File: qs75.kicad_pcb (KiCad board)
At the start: 2 copper layers, 285 x 95.1 mm, 284 parts, among them J1 SWD, J2 SPI, J3 UART, J4 USB2.0, J5 PB14, SW1 SW_Push, SW10 1u, SW11 1u, SW12 1u, SW13 1u, SW14 1u, SW15 1u, SW16 1u, SW17 1u, SW18 1u, SW19 1u, SW2 1u, SW20 1u, SW21 1u, SW22 1u, SW23 1u, SW24 1u, SW25 1u, SW26 1u, SW27 1u, SW28 1u, SW29 1u, SW3 1u, SW30 1u, SW31 1u, SW32 1u, SW33 1u, SW34 1u, SW35 1u, SW36 1u, SW37 1u, SW38 1u, SW39 1u, SW4 1u, SW40 1u, SW41 1u, SW42 1u, SW43 1u, SW44 1u, SW45 1u, SW46 1u, SW47 1u, SW48 1u, SW49 1u, SW5 1u, SW50 1u, SW51 1u, SW52 1u, SW53 1u, SW54 1u, SW55 1u, SW56 1u, SW57 1u, SW58 1u, SW59 1u, SW6 1u, SW60 1u, SW61 1u, SW62 1u, SW63 1u, SW64 1u, SW65 1u, SW66 1u, SW67 1u, SW68 1u, SW69 1u, SW7 1u, SW70 1u, SW71 1u, SW72 1u, SW73 1u, SW74 1u, SW75 1u, SW76 1u, SW77 SW_Push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

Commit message: Delete gerbers
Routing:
- added copper zone on F.Cu, net GND
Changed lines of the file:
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@@
   (via (at 206.9125 90.6375) (size 0.8) (drill 0.4) (layers F.Cu B.Cu) (net 2))
   (via (at 200.6625 88.5875) (size 0.8) (drill 0.4) (layers F.Cu B.Cu) (net 2))
-  (via (at 187.8125 90.1375) (size 0.8) (drill 0.4) (layers F.Cu B.Cu) (net 53))
   (via (at 181.7625 88.6875) (size 0.8) (drill 0.4) (layers F.Cu B.Cu) (net 2))
   (via (at 187.8625 70.9875) (size 0.8) (drill 0.4) (layers F.Cu B.Cu) (net 2))
@@
   (segment (start 134.406249 97.743751) (end 132.9625 99.1875) (width 0.25) (layer F.Cu) (net 52))
   (segment (start 134.956249 97.743751) (end 134.406249 97.743751) (width 0.25) (layer F.Cu) (net 52))
+  (via (at 187.8125 90.1375) (size 0.8) (drill 0.4) (layers F.Cu B.Cu) (net 53))
   (via (at 170.7125 99.1375) (size 0.8) (drill 0.4) (layers F.Cu B.Cu) (net 53) (status 30))
   (segment (start 179.4795 37.8445) (end 180.0555 37.8445) (width 0.25) (layer B.Cu) (net 53) (status 10))
@@
     (connect_pads (clearance 0.30734))
     (min_thickness 0.254)
+    (fill yes (arc_segments 32) (thermal_gap 0.508) (thermal_bridge_width 0.508))
+    (polygon
+      (pts
+        (xy 6.7 19.9) (xy 291.7 19.9) (xy 291.7 114.5) (xy 6.7 114.5)
+      )
+    )
+  )
+  (zone (net 2) (net_name GND) (layer F.Cu) (hatch edge 0.508)
+    (connect_pads (clearance 0.30734))
+    (min_thickness 0.254)

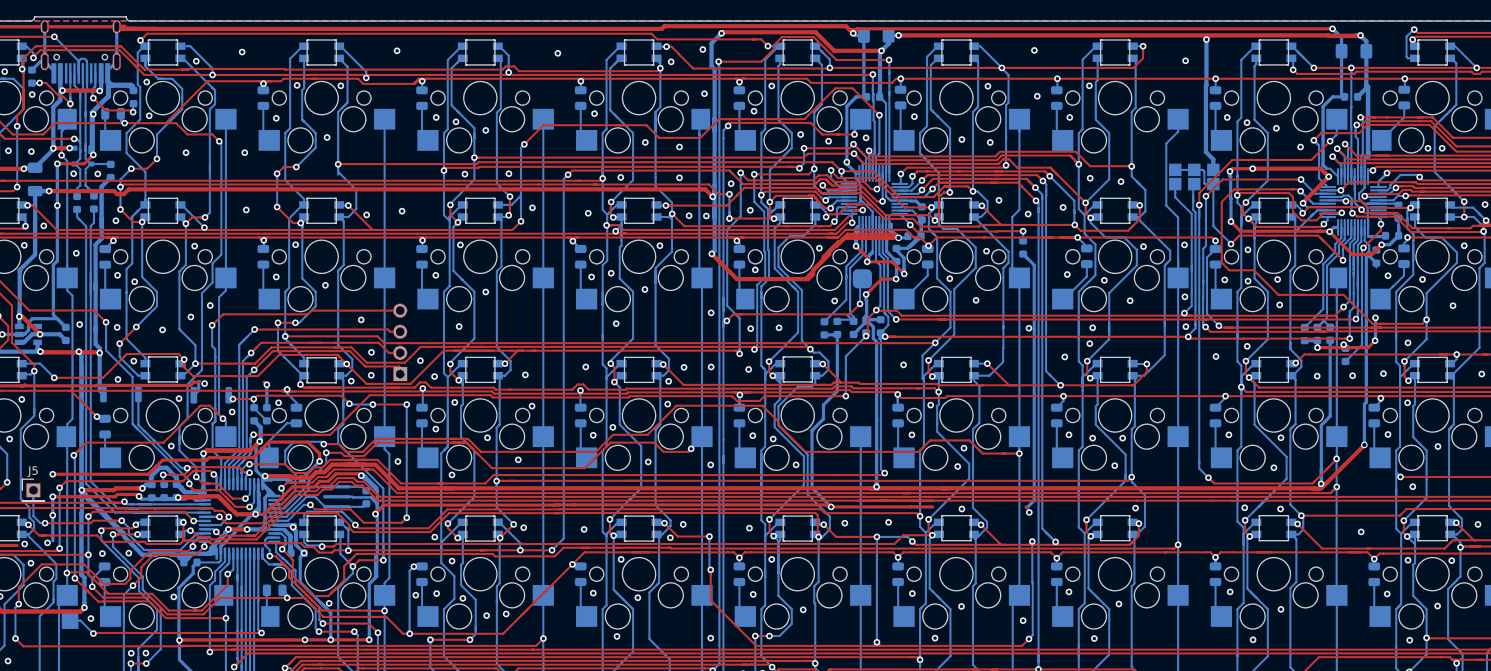
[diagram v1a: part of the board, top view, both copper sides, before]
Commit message: add tracks
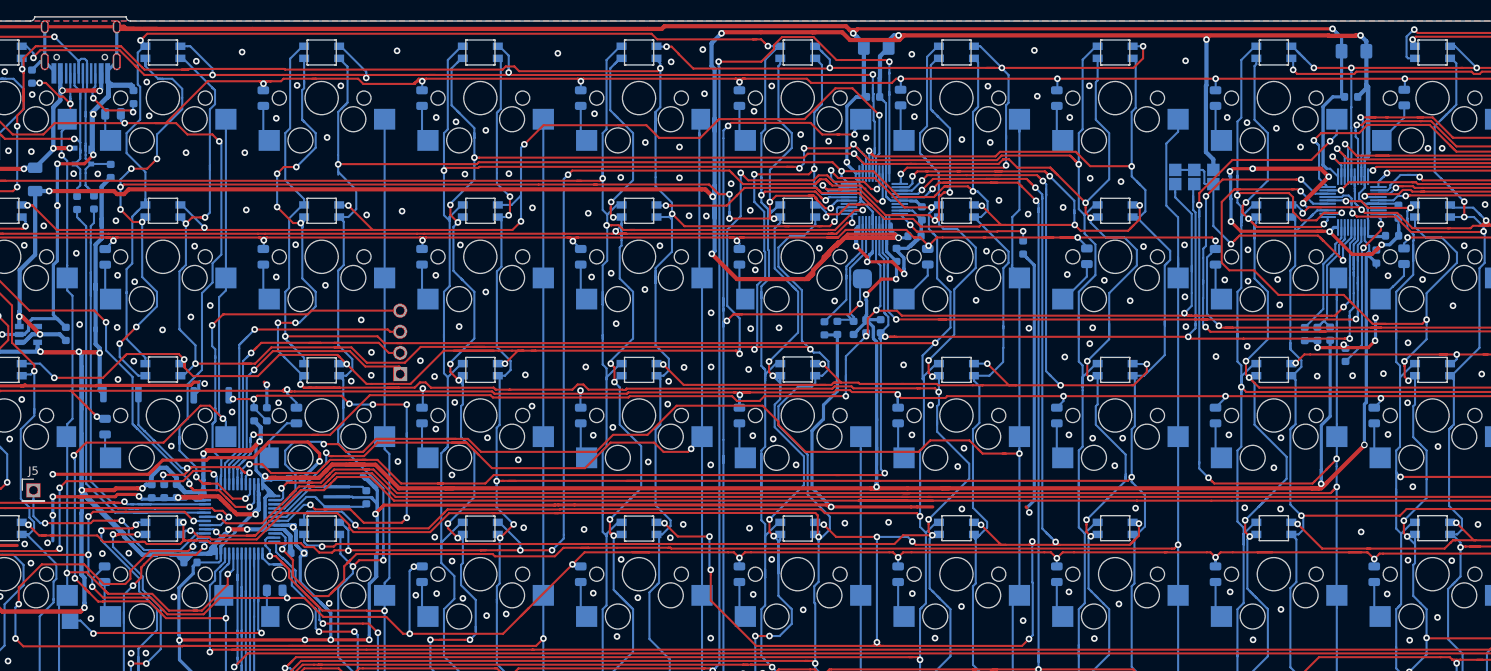
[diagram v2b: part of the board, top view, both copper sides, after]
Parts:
- moved C11 1.45 mm to (120.4, 23.1)
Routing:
- net GND: track 1041.9 -> 1020.4 mm, vias 440 -> 441
- net +3V3: track 670.7 -> 662.4 mm
- net COL11: track 285.8 -> 293.1 mm
- net +5V: track 425.3 -> 429.5 mm, vias 11 -> 10
- net SDA: track 213.2 -> 215.1 mm
- net COL12: track 295.0 -> 296.5 mm
- net COL4: track 140.2 -> 141.0 mm
- net COL8: track 269.6 -> 270.2 mm
- net bCS5: vias 9 -> 8
